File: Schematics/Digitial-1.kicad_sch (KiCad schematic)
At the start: 18 parts, among them J30 Conn_01x02, J31 To Compute #1, U19 LM1117-5.0, U20 LM1117-3.3, U21 USB Host Shield 2.0, U22 ESP32-DEVKIT-V1

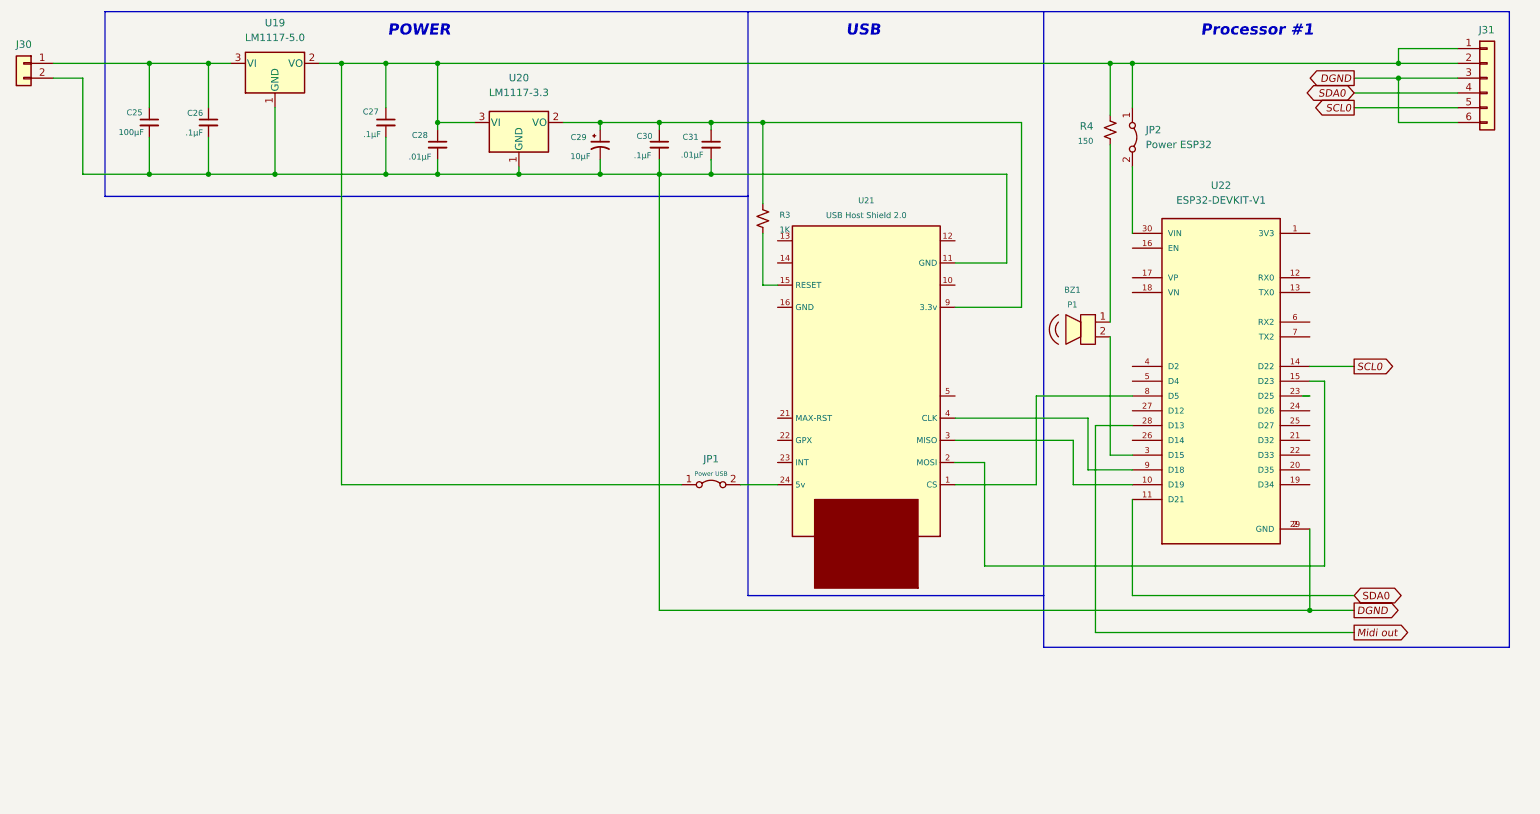
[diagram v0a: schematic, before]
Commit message: Now with dual ESP32 with Midi32 and Disp32.
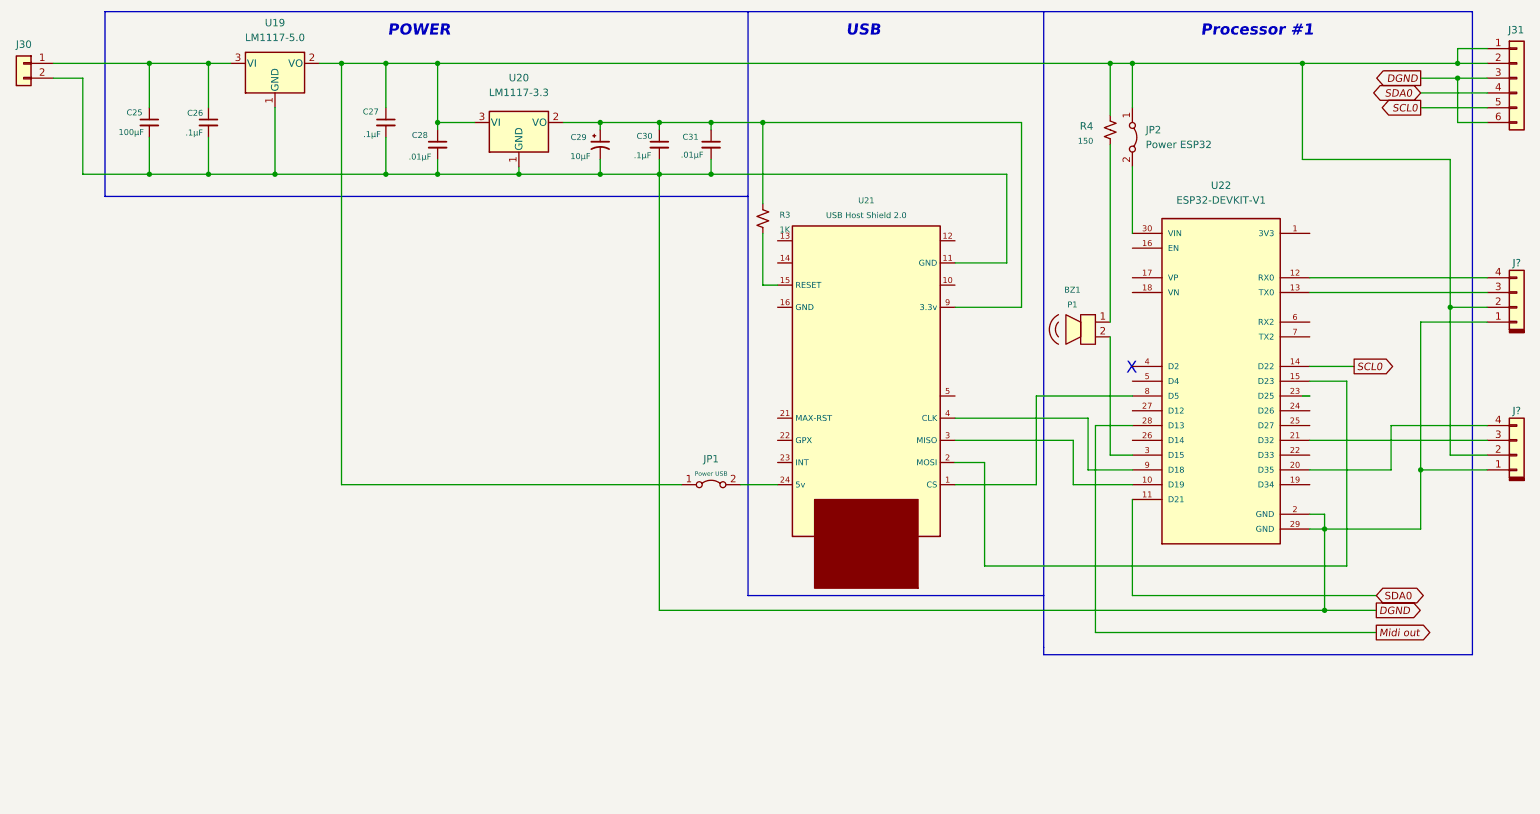
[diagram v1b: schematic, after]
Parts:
- added J? (x2): Conn_01x04, symbol Connector_keyed_kicad_sym:Conn_01x04
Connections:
- net DGND: now also J?.1 (Pin_1), J?.1 (Pin_1)
- net at U22.12 (RX0): now also J?.4 (Pin_4)
- net at U22.13 (TX0): now also J?.3 (Pin_3)
- net at U22.20 (D35): now also J?.4 (Pin_4)
- net at U22.21 (D32): now also J?.3 (Pin_3)
- net at C27.1, C28.1, J31.1 (Pin_1)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: now also J?.2 (Pin_2), J?.2 (Pin_2)
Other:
- note added: "X"
- moved on the sheet: J31

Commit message: Disp32 interface working properly.
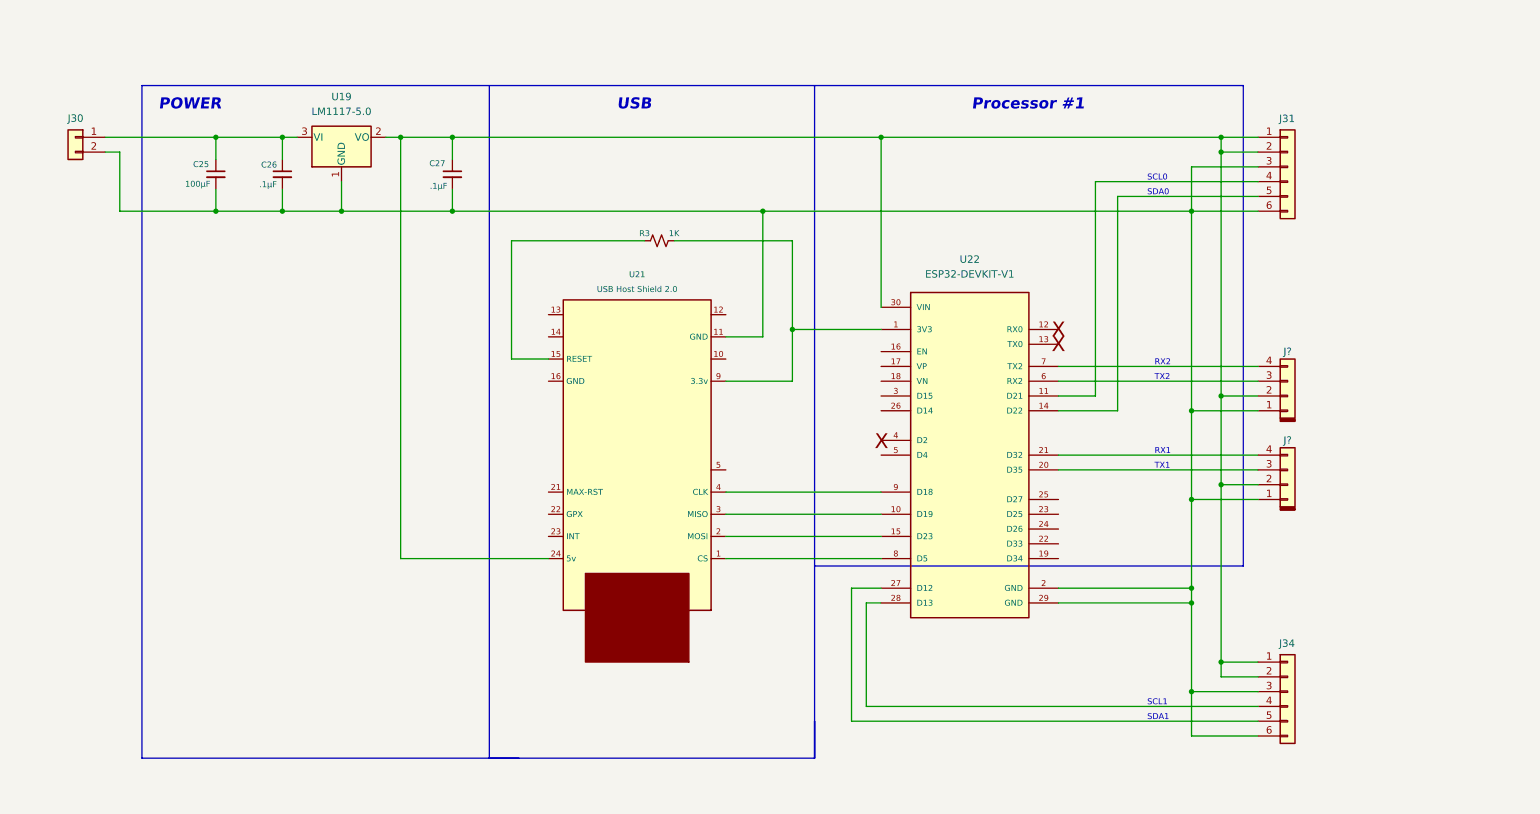
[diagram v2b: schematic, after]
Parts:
- removed BZ1: P1, digikey-footprints:Piezo_9x9mm_PKMCS0909E4000-R1, symbol dk_Alarms-Buzzers-and-Sirens:PKMCS0909E4000-R1
- removed C28, C31: .01µF, symbol Device:C_Small
- removed C29: 10µF, symbol Device:C_Polarized_Small_US
- removed C30: .1µF, symbol Device:C_Small
- removed JP1: Power USB, symbol Jumper:Jumper_2_Bridged
- removed JP2: Power ESP32, symbol Jumper:Jumper_2_Bridged
- removed R4: 150, symbol Device:R_Small_US
- removed U20: LM1117-3.3, symbol Regulator_Linear:LM1117-3.3
- added J34: To Compute #1, symbol Connector_Generic:Conn_01x06
- U22: footprint MODULE_ESP32_DEVKIT_V1 -> (none); MANUFACTURER DOIT -> (none); MAXIMUM_PACKAGE_HEIGHT 6.8 mm -> (none); PARTREV N/A -> (none); STANDARD Manufacturer Recommendations -> (none)
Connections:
- net at U22.1 (3V3): now also R3.1, U21.9 (3.3v)
- net at U22.12 (RX0): no longer J?.4 (Pin_4)
- net at U22.13 (TX0): no longer J?.3 (Pin_3)
- net at U22.20 (D35): now also J?.3 (Pin_3); no longer J?.4 (Pin_4)
- net at U22.21 (D32): now also J?.4 (Pin_4); no longer J?.3 (Pin_3)
- net at U22.27 (D12): now also J34.5 (Pin_5)
- net at U22.30 (VIN): now also C27.1, J31.1 (Pin_1), J31.2 (Pin_2), J?.2 (Pin_2), J?.2 (Pin_2), U19.2 (VO), U21.24 (5v), J34.1 (Pin_1), J34.2 (Pin_2)
- net at U22.6 (RX2): now also J?.3 (Pin_3)
- net at U22.7 (TX2): now also J?.4 (Pin_4)
- net DGND: no longer names the net of C25.2, C26.2, C27.2, J30.2 (Pin_2), J31.3 (Pin_3), J31.6 (Pin_6), J?.1 (Pin_1), J?.1 (Pin_1), U19.1 (GND), U21.11 (GND), U22.2 (GND), U22.29 (GND)
- net DGND: now also J34.3 (Pin_3), J34.6 (Pin_6)
- net Midi out: no longer names the net of U22.28 (D13)
- net Midi out: now also J34.4 (Pin_4)
- net SCL0: no longer names the net of J31.5 (Pin_5), U22.14 (D22)
- net SDA0: no longer names the net of J31.4 (Pin_4), U22.11 (D21)
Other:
- note added: "RX1"
- note added: "RX2"
- note added: "SCL0"
- note added: "SCL1"
- note added: "SDA0"
- note added: "SDA1"
- note added: "TX1"
- note added: "TX2"
- note removed: "X"
- moved on the sheet: C25, C26, C27, J30, J31, J?, U19, U21

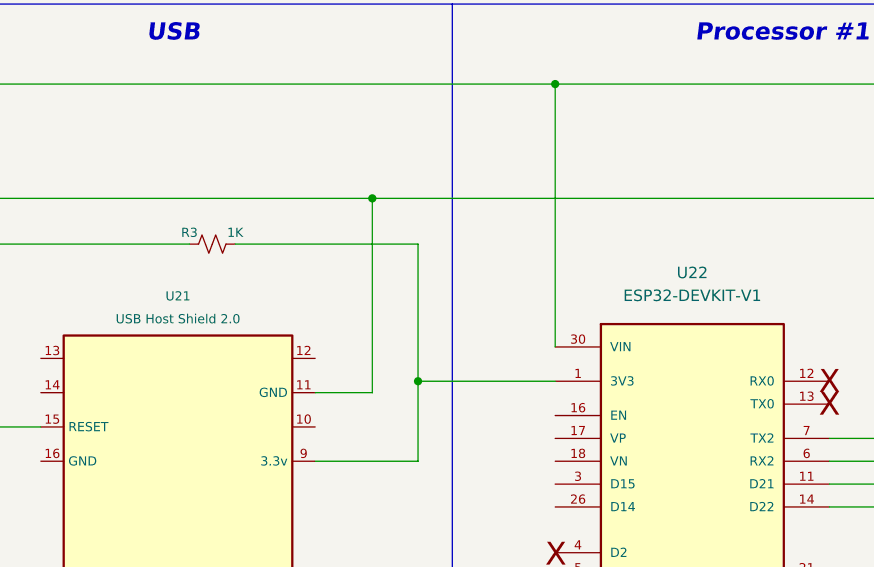
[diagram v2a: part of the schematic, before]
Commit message: adding noise source and variable state filter.
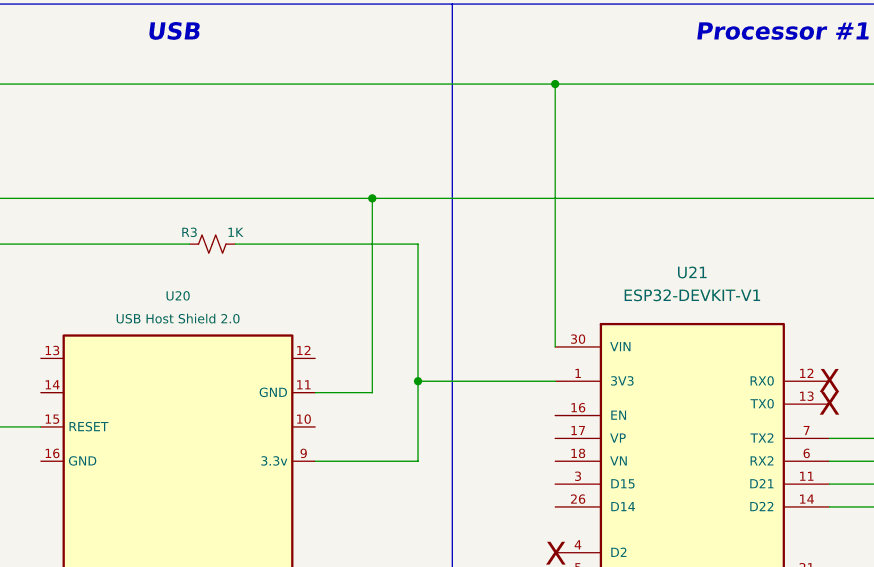
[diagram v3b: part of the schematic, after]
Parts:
- renumbered U21 to U20, U22 to U21
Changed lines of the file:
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@@
   (symbol (lib_id "ESP32-DEVKIT-V1:ESP32-DEVKIT-V1") (at 222.25 92.71 0) (unit 1)
     (in_bom yes) (on_board yes) (dnp no) (fields_autoplaced)
-    (property "Reference" "U22" (at 222.25 59.0804 0)
+    (property "Reference" "U21" (at 222.25 59.0804 0)
       (effects (font (size 1.27 1.27)))
     )
@@
       (project "Schematics-Midi32"
         (path "/718f017d-28fe-4e29-b548-40db8e21cec7/5f23d779-3412-4b06-96f4-480c60744fb9"
-          (reference "U22") (unit 1)
+          (reference "U21") (unit 1)
         )
       )
@@
   (symbol (lib_id "Module-Max3421EE:USB Host Shield 2.0") (at 165.1 93.98 180) (unit 1)
     (in_bom yes) (on_board yes) (dnp no) (fields_autoplaced)
-    (property "Reference" "U21" (at 165.1 61.6712 0)
+    (property "Reference" "U20" (at 165.1 61.6712 0)
       (effects (font (size 1.016 1.016)))
     )
@@
       (project "Schematics-Midi32"
         (path "/718f017d-28fe-4e29-b548-40db8e21cec7/5f23d779-3412-4b06-96f4-480c60744fb9"
-          (reference "U21") (unit 1)
-        )
-      )
+          (reference "U20") (unit 1)
+        )
+      )

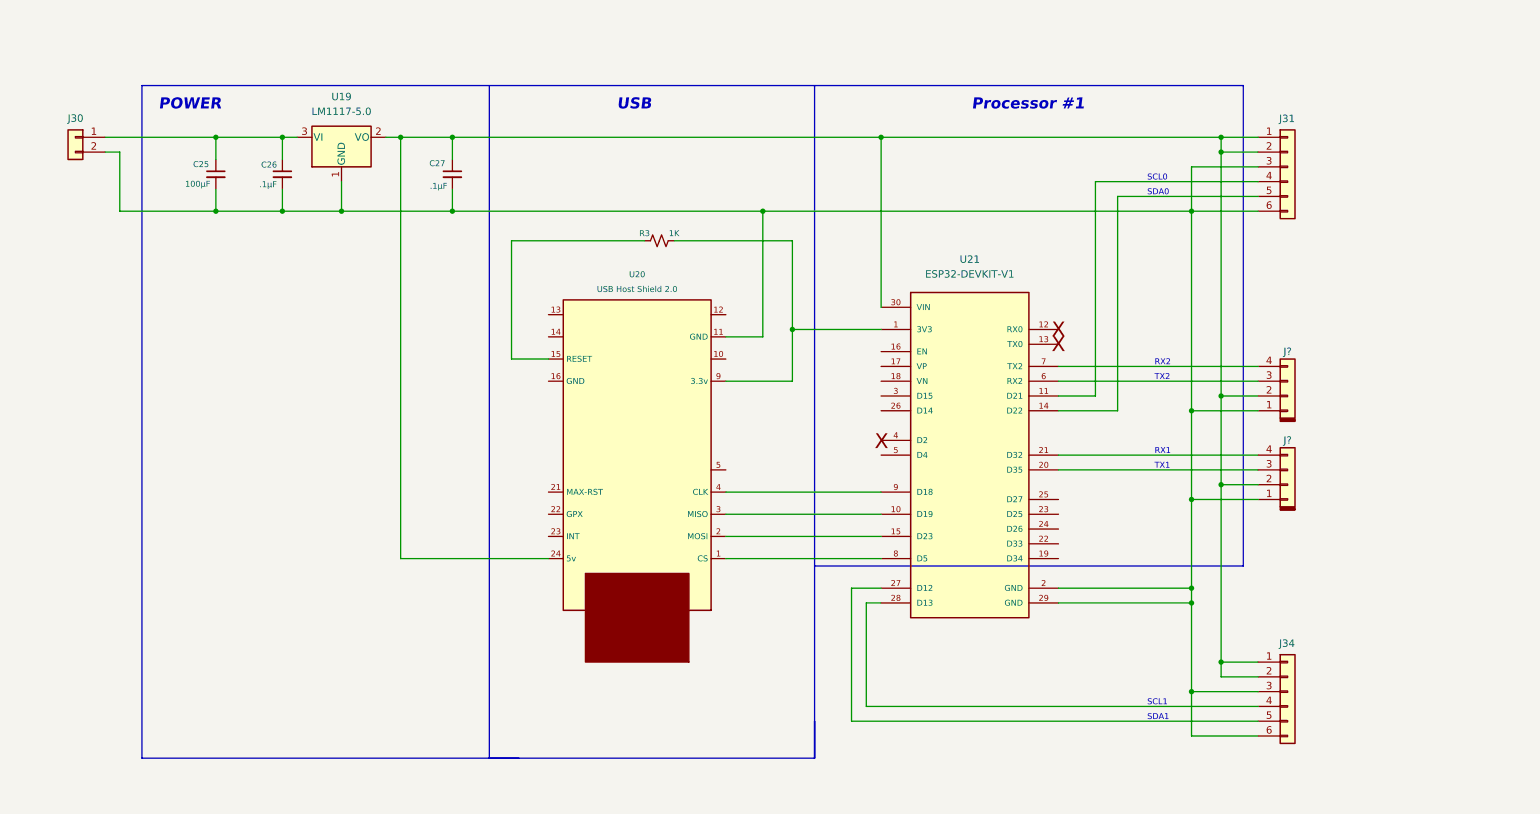
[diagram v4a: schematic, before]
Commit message: Partial software with complete hardware on best 3 state filter with 4 outputs.
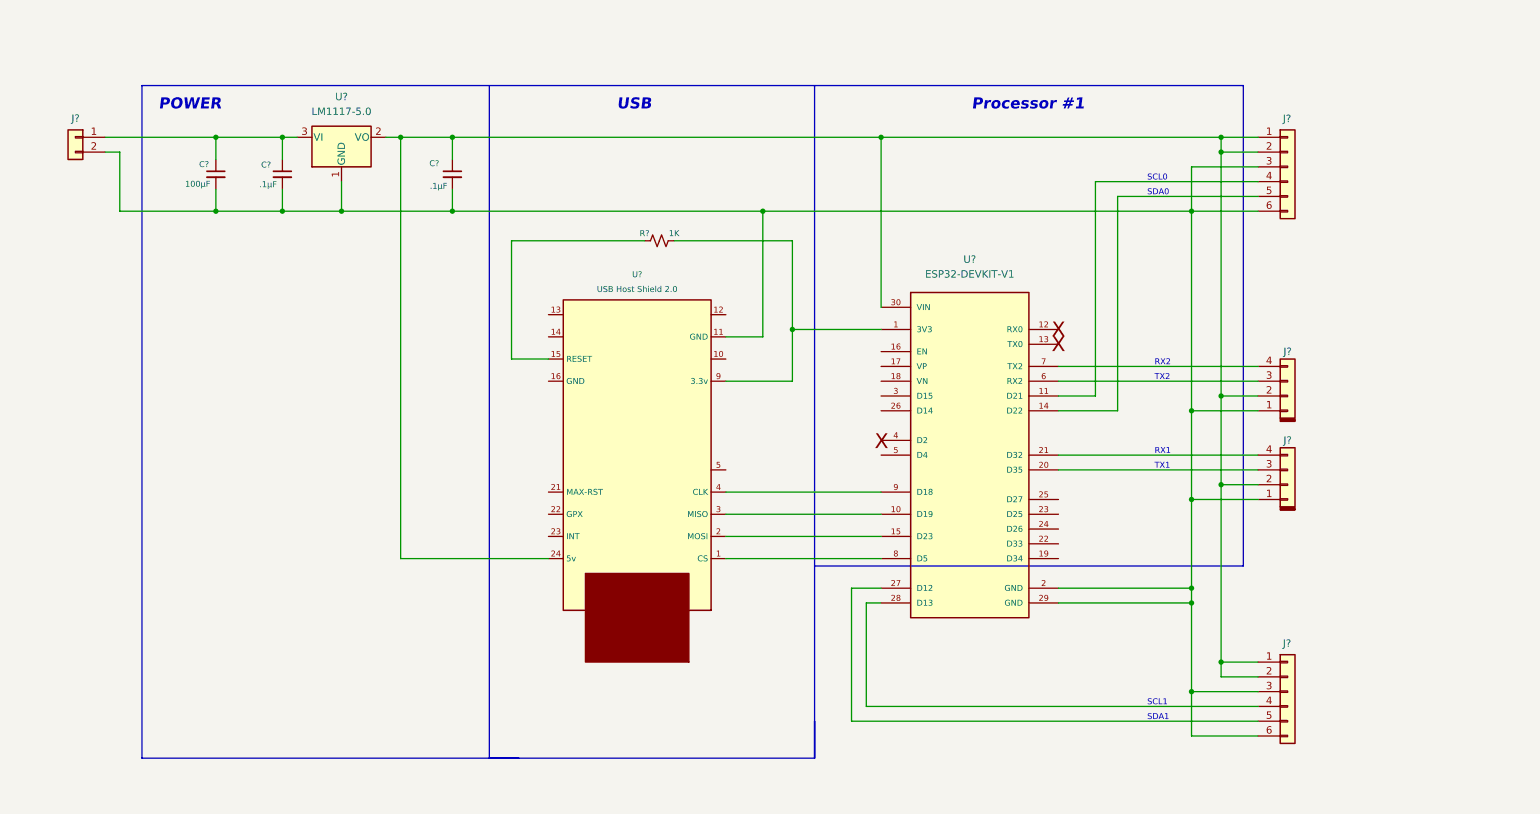
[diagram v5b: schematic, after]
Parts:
- renumbered C26 to C?, C25 to C?, C27 to C?, J31 to J?, J30 to J?, J34 to J?, R3 to R?, U21 to U?, U19 to U?, U20 to U?

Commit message: - Updated current libraries - New 7 inc display with ESP32S3 and second USB upload port - Start of I2C feeder interface slave on display.
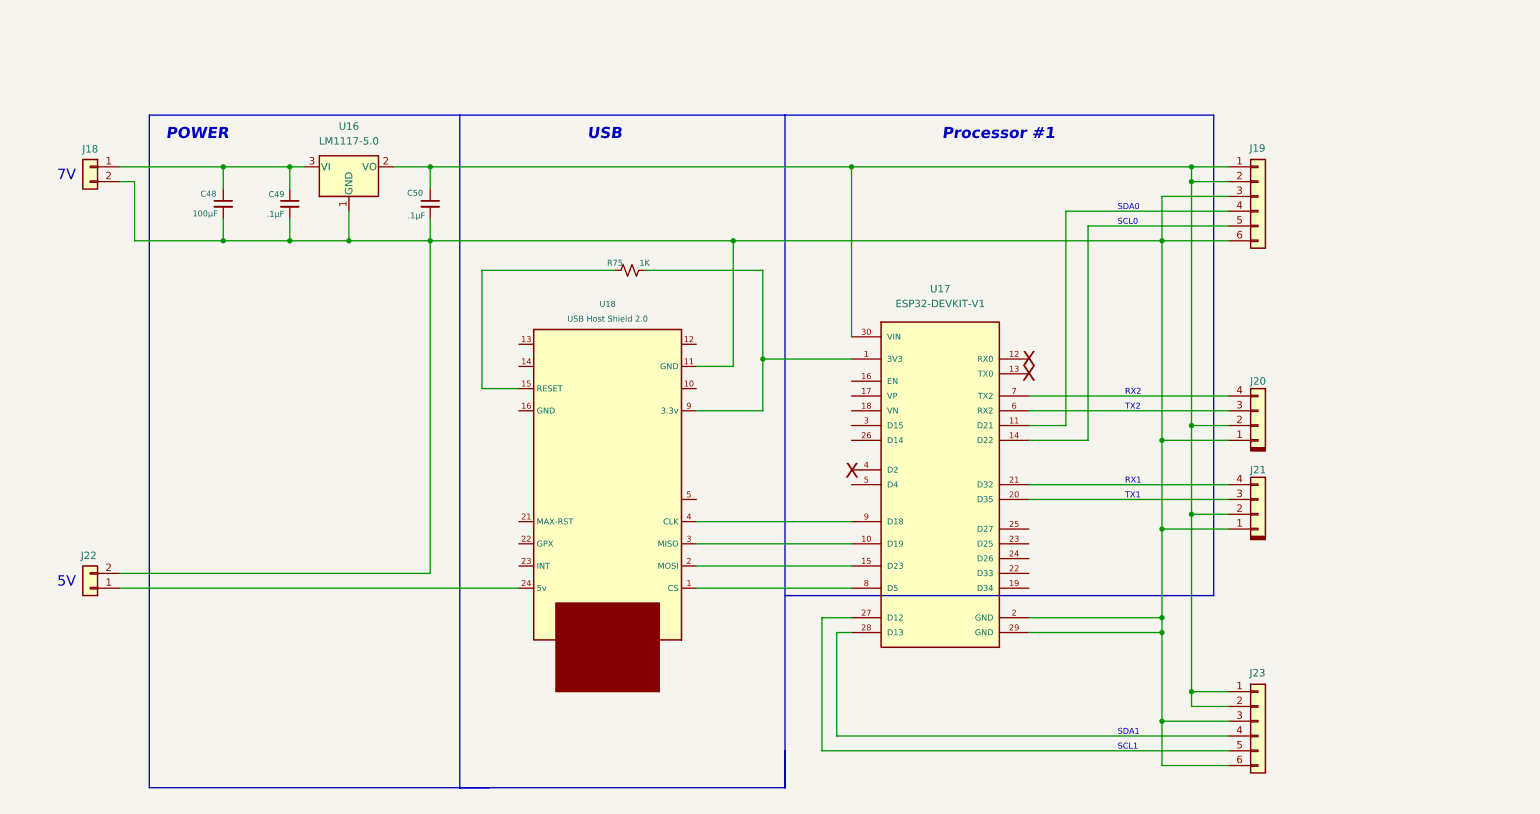
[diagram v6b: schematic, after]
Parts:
- added J22: Conn_01x02, symbol Connector_Generic:Conn_01x02
- gave numbers to parts that had none: 12
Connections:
- net at C48.2, C49.2, C50.2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: now also J22.2 (Pin_2)
- net at C50.1, J19.1 (Pin_1), J19.2 (Pin_2)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: no longer U18.24 (5v)
- new net: J22.1 (Pin_1), U18.24 (5v)
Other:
- note added: "5V"
- note added: "7V"
- moved on the sheet: C48, C49, C50, J18, J19, J20, J21, J23, R75, U16, U17, U18
